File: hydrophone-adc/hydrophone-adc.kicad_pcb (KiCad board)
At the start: 4 copper layers, 204 parts, among them J1001 TEST_1P, J1002 TEST_1P, J1003 TEST_1P, J1004 TEST_1P, J1005 TEST_1P, J1006 TEST_1P, J1007 TEST_1P, J1101 TEST_1P, J1102 TEST_1P, J1201 TEST_1P, J1202 TEST_1P, J1203 TEST_1P, J1204 TEST_1P, J1205 TEST_1P, J1206 TEST_1P, J1207 TEST_1P, J1301 BARREL_JACK, J401 CONN_COAXIAL, J402 CONN_COAXIAL, J403 CONN_COAXIAL, J404 CONN_COAXIAL, J405 TEST_1P, J406 TEST_1P, J407 TEST_1P, J408 TEST_1P, J409 TEST_1P, J410 TEST_1P, J411 TEST_1P, J412 TEST_1P, J501 TEST_1P, J502 TEST_1P, J601 TEST_1P, J602 TEST_1P, J603 TEST_1P, J604 TEST_1P, J605 TEST_1P, J606 TEST_1P, J607 TEST_1P, J701 TEST_1P, J702 TEST_1P, J801 TEST_1P, J802 TEST_1P, J803 TEST_1P, J804 TEST_1P, J805 TEST_1P, J806 TEST_1P, J807 TEST_1P, J901 TEST_1P, J902 TEST_1P, U1001 LM324, U1101 el5170, U1201 LM324, U1301 TS30013, U1302 LM2776, U1303 LT1963, U201 micro-zed-jx1, U301 micro-zed-jx2, U401 LTC2171-14, U501 el5170, U601 LM324, U701 el5170, U801 LM324, U901 el5170

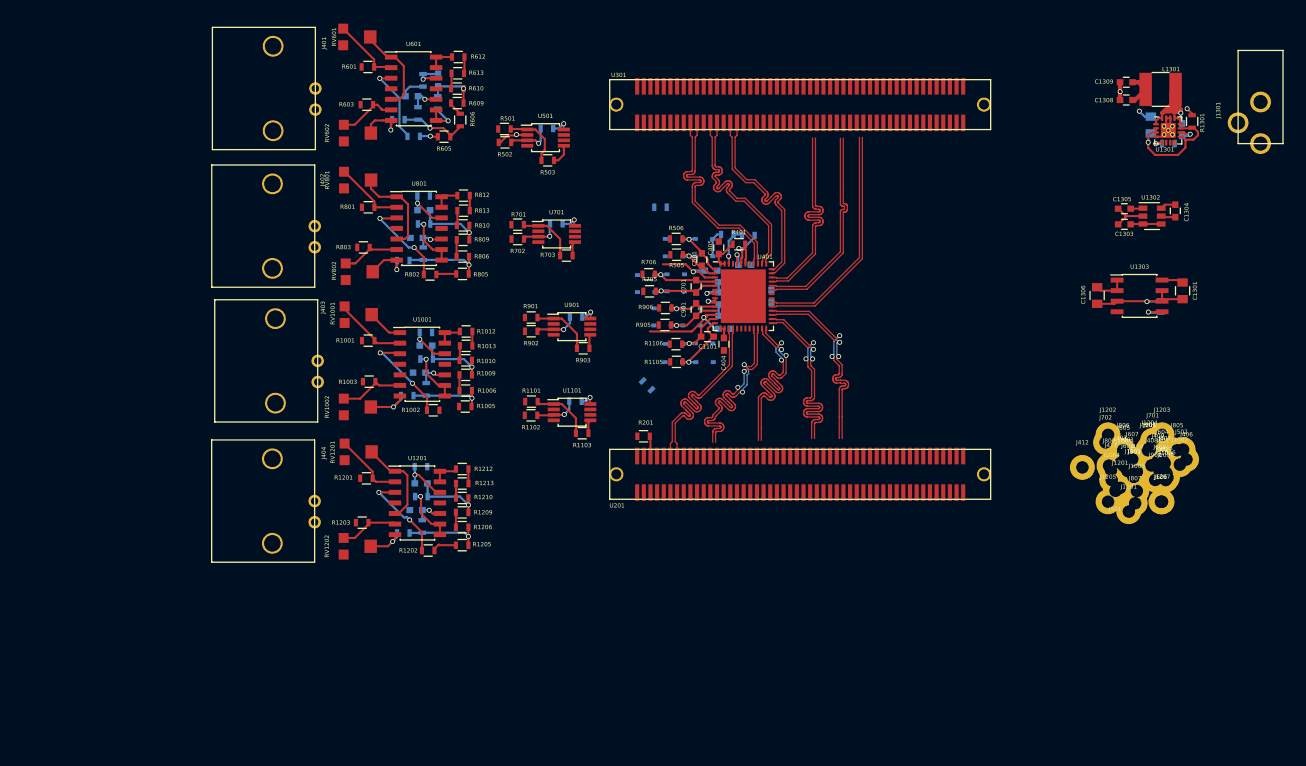
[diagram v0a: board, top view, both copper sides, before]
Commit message: Finished differential routing and plane layout
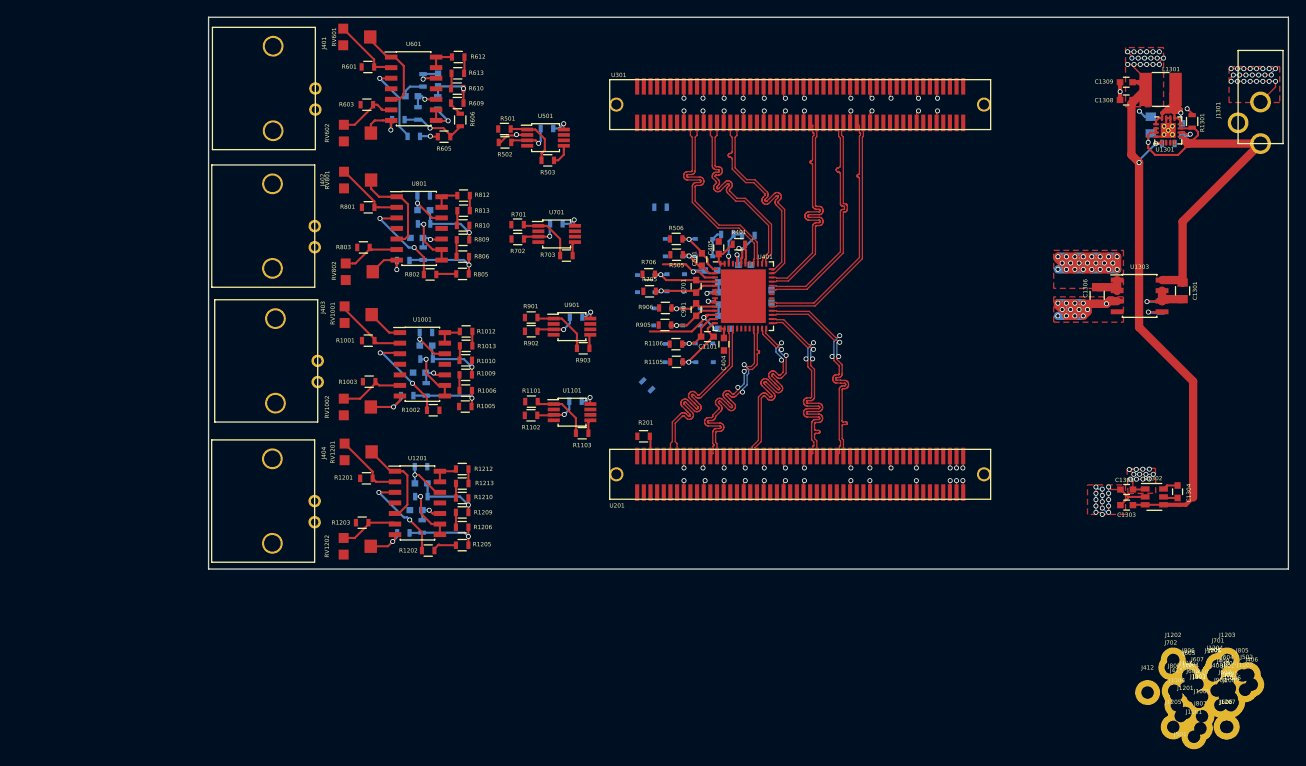
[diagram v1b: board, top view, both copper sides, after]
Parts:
- moved C1304 33.8 mm to (223.2, 97.3)
- moved C1305 33.8 mm to (217.1, 97.1)
- moved C1303 33.8 mm to (217.1, 99.0)
- moved U1302 33.8 mm to (220.4, 98.0)
- moved J1001 28.2 mm to (224.8, 121.2)
- moved J1002 28.2 mm to (231.3, 121.2)
- moved J1005 28.2 mm to (226.1, 124.3)
- moved J1006 28.2 mm to (229.8, 122.7)
- moved J1007 28.2 mm to (224.6, 121.4)
- moved J1204 28.2 mm to (227.7, 119.1)
- moved J1205 28.2 mm to (222.7, 125.6)
- moved J1206 28.2 mm to (227.4, 119.4)
- moved J1207 28.2 mm to (229.1, 125.6)
- moved J406 28.2 mm to (232.1, 120.5)
- moved J502 28.2 mm to (231.7, 119.3)
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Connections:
- U201 pad 23: (no net) -> /out4b+
- U201 pad 25: (no net) -> /out4b-
- U201 pad 35: (no net) -> /out4a+
- U201 pad 37: (no net) -> /out4a-
- U201 pad 53: (no net) -> /out3b+
- U201 pad 55: (no net) -> /out3b-
- U201 pad 61: (no net) -> /out3a+
- U201 pad 63: (no net) -> /out3a-
- U301 pad 36: /out2b+ -> (no net)
- U301 pad 38: /out2b- -> (no net)
- U301 pad 42: /data_clk+ -> (no net)
- U301 pad 44: /data_clk- -> (no net)
- U301 pad 54: (no net) -> /out2b+
- U301 pad 56: (no net) -> /out2b-
- U301 pad 62: /fr_clk+ -> /data_clk+
- U301 pad 64: /fr_clk- -> /data_clk-
- U301 pad 68: /out3a+ -> /fr_clk+
- U301 pad 70: /out3a- -> /fr_clk-
- U301 pad 74: /out3b+ -> (no net)
- U301 pad 76: /out3b- -> (no net)
- U301 pad 82: /out4a+ -> (no net)
- U301 pad 84: /out4a- -> (no net)
- U301 pad 88: /out4b+ -> (no net)
- U301 pad 90: /out4b- -> (no net)
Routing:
- net GND: track 31.5 -> 147.7 mm, vias 5 -> 106
- net +5V: track 9.33 -> 86.7 mm, vias 1 -> 20
- net /Power/Vin: track 18.3 -> 48.3 mm
- net +1V8: track 12.7 -> 36.6 mm, vias 0 -> 23
- net -5V: track 1.50 -> 11.5 mm, vias 0 -> 12
- net /out3b-: track 24.2 -> 27.5 mm
- net /out3a-: track 24.3 -> 27.5 mm
- net /data_clk+: track 24.4 -> 27.0 mm
- net /out2b+: track 24.4 -> 26.9 mm
- net /out3b+: track 25.0 -> 27.5 mm
- net /out3a+: track 25.1 -> 27.5 mm
- net /fr_clk+: track 27.3 -> 29.7 mm
- net /out4a-: track 24.4 -> 26.7 mm
- net /out4a+: track 24.4 -> 26.7 mm
- net /out4b+: track 24.5 -> 26.7 mm
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- added copper zone on F.Cu, net +1V8
- added copper zone on In2.Cu, net +1V8
- added copper zone on F.Cu, net +5V
- added copper zone on In2.Cu, net +5V
- added copper zone on F.Cu, net -5V
- added copper zone on In2.Cu, net -5V
- added copper zone on F.Cu, net GND
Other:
- board outline added: 129.8 x 66.3 mm

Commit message: DRC is now passing and preliminary layout is complete.
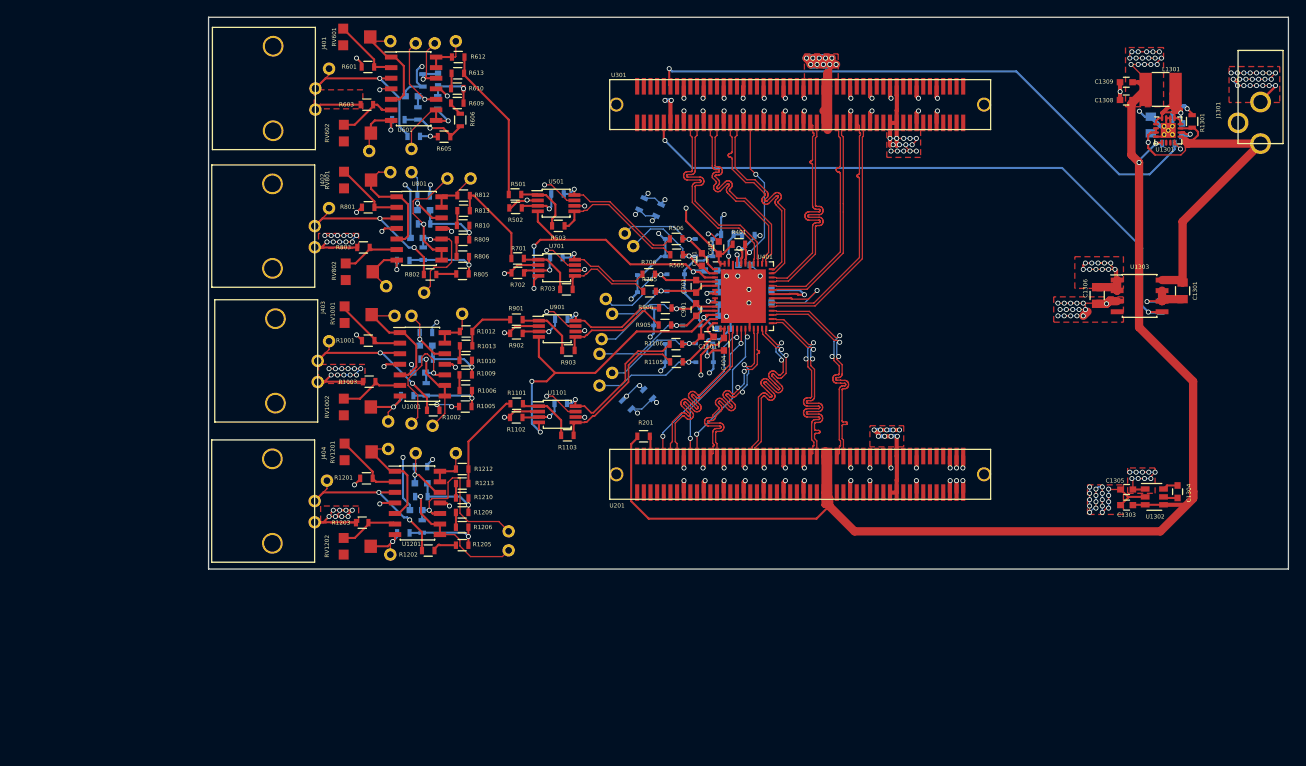
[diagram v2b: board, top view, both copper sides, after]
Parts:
- removed J405, J406, J407, J408, J409, J410, J411, J412: TEST_1P, Measurement_Points:Measurement_Point_Round-TH_Big
- added L403: Ferrite_Bead, Resistors_SMD:R_0603, B.Cu at (157.0, 86.9)
- added L404: Ferrite_Bead, Resistors_SMD:R_0603, B.Cu at (158.8, 62.7)
- J1001, J1002, J1003, J1004, J1005, J1006, J1007, J1101, J1102, J1201, J1202, J1203, J1204, J1205, J1206, J1207, J501, J502, J601, J602, J603, J604, J605, J606, J607, J701, J702, J801, J802, J803, J804, J805, J806, J807, J901, J902: footprint Measurement_Points:Measurement_Point_Round-TH_Big -> Measurement_Points:Measurement_Point_Round-TH_Small
- moved J601 129.1 mm to (121.2, 46.5)
- moved J602 127.6 mm to (128.5, 43.2)
- moved J606 125.7 mm to (133.9, 43.4)
- moved J604 124.2 mm to (131.6, 43.4)
- moved J801 122.7 mm to (121.2, 63.2)
- moved J603 118.7 mm to (126.0, 56.4)
- moved J607 118.0 mm to (136.4, 43.2)
- moved J605 113.1 mm to (131.1, 56.1)
- moved J802 113.0 mm to (128.5, 58.9)
- moved J805 112.7 mm to (135.4, 59.7)
- moved J1001 111.8 mm to (121.2, 79.2)
- moved J1002 111.7 mm to (129.0, 76.2)
- moved J806 111.3 mm to (131.1, 58.9)
- moved J807 109.9 mm to (138.2, 59.7)
- moved J803 109.8 mm to (128.0, 72.6)
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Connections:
- net /ADC/Diff Conv1/Vout+ renamed /ADC/v1+
- net /ADC/Diff Conv1/Vout- renamed /ADC/v1-
- net /ADC/Diff Conv2/Vout+ renamed /ADC/v2+
- net /ADC/Diff Conv2/Vout- renamed /ADC/v2-
- net /ADC/Diff Conv3/Vout+ renamed /ADC/v3+
- net /ADC/Diff Conv3/Vout- renamed /ADC/v3-
- net /ADC/Diff Conv4/Vout+ renamed /ADC/v4+
- net /ADC/Diff Conv4/Vout- renamed /ADC/v4-
- net Net-(R1103-Pad1) renamed /ADC/Diff Conv4/v+
- net Net-(R1104-Pad1) renamed /ADC/Diff Conv4/v-
- net Net-(R503-Pad1) renamed /ADC/Diff Conv1/v+
- net Net-(R504-Pad1) renamed /ADC/Diff Conv1/v-
- net Net-(R703-Pad1) renamed /ADC/Diff Conv2/v+
- net Net-(R704-Pad1) renamed /ADC/Diff Conv2/v-
- net Net-(R903-Pad1) renamed /ADC/Diff Conv3/v+
- net Net-(R904-Pad1) renamed /ADC/Diff Conv3/v-
- J1301 pad 3: (no net) -> Net-(J1301-Pad3)
- R401 pad 2: /ADC/MISO -> /MISO
- RV1001 pad 3: (no net) -> Net-(RV1001-Pad3)
- RV1002 pad 3: (no net) -> Net-(RV1002-Pad3)
- RV1201 pad 3: (no net) -> Net-(RV1201-Pad3)
- RV1202 pad 3: (no net) -> Net-(RV1202-Pad3)
- RV601 pad 3: (no net) -> Net-(RV601-Pad3)
- RV602 pad 3: (no net) -> Net-(RV602-Pad3)
- RV801 pad 3: (no net) -> Net-(RV801-Pad3)
- RV802 pad 3: (no net) -> Net-(RV802-Pad3)
- U201 pad 1: (no net) -> Net-(U201-Pad1)
- U201 pad 10: (no net) -> /MicroZed-JX1/SE1
- U201 pad 12: (no net) -> Net-(U201-Pad12)
- U201 pad 14: (no net) -> Net-(U201-Pad14)
- U201 pad 17: (no net) -> /SCK
- U201 pad 18: (no net) -> Net-(U201-Pad18)
- U201 pad 19: (no net) -> /MOSI
- U201 pad 2: (no net) -> Net-(U201-Pad2)
- U201 pad 20: (no net) -> Net-(U201-Pad20)
- U201 pad 24: (no net) -> Net-(U201-Pad24)
- U201 pad 26: (no net) -> Net-(U201-Pad26)
- U201 pad 29: (no net) -> /MicroZed-JX1/LVDS6+
- U201 pad 3: (no net) -> Net-(U201-Pad3)
- U201 pad 30: (no net) -> Net-(U201-Pad30)
- U201 pad 31: (no net) -> /MicroZed-JX1/LVDS6-
- U201 pad 32: (no net) -> Net-(U201-Pad32)
- U201 pad 36: (no net) -> Net-(U201-Pad36)
- U201 pad 38: (no net) -> Net-(U201-Pad38)
- U201 pad 4: (no net) -> Net-(U201-Pad4)
- U201 pad 41: (no net) -> /MicroZed-JX1/LVDS10+
- U201 pad 42: (no net) -> Net-(U201-Pad42)
- U201 pad 43: (no net) -> /MicroZed-JX1/LVDS10-
- U201 pad 44: (no net) -> Net-(U201-Pad44)
- U201 pad 47: (no net) -> /MicroZed-JX1/LVDS12+
- U201 pad 48: (no net) -> Net-(U201-Pad48)
- U201 pad 49: (no net) -> /MicroZed-JX1/LVDS12-
- U201 pad 50: (no net) -> Net-(U201-Pad50)
- U201 pad 54: (no net) -> Net-(U201-Pad54)
- U201 pad 56: (no net) -> Net-(U201-Pad56)
- U201 pad 6: (no net) -> Net-(U201-Pad6)
- U201 pad 62: (no net) -> Net-(U201-Pad62)
- U201 pad 64: (no net) -> Net-(U201-Pad64)
- U201 pad 67: (no net) -> /MicroZed-JX1/LVDS18+
- U201 pad 68: (no net) -> Net-(U201-Pad68)
- U201 pad 69: (no net) -> /MicroZed-JX1/LVDS18-
- U201 pad 7: (no net) -> Net-(U201-Pad7)
- U201 pad 70: (no net) -> Net-(U201-Pad70)
- U201 pad 73: (no net) -> /MicroZed-JX1/LVDS20+
- U201 pad 74: (no net) -> Net-(U201-Pad74)
- U201 pad 75: (no net) -> /MicroZed-JX1/LVDS20-
- U201 pad 76: (no net) -> Net-(U201-Pad76)
- U201 pad 8: (no net) -> Net-(U201-Pad8)
- U201 pad 81: (no net) -> Net-(U201-Pad81)
- U201 pad 82: (no net) -> Net-(U201-Pad82)
- U201 pad 83: (no net) -> Net-(U201-Pad83)
- U201 pad 84: (no net) -> Net-(U201-Pad84)
- U201 pad 87: (no net) -> Net-(U201-Pad87)
- U201 pad 88: (no net) -> Net-(U201-Pad88)
- U201 pad 89: (no net) -> Net-(U201-Pad89)
- U201 pad 9: (no net) -> /~CS
- U201 pad 90: (no net) -> Net-(U201-Pad90)
- U201 pad 91: (no net) -> Net-(U201-Pad91)
- U201 pad 92: (no net) -> Net-(U201-Pad92)
- U201 pad 93: (no net) -> Net-(U201-Pad93)
- U201 pad 94: (no net) -> Net-(U201-Pad94)
- U301 pad 1: (no net) -> Net-(U301-Pad1)
- U301 pad 100: (no net) -> Net-(U301-Pad100)
- U301 pad 13: (no net) -> Net-(U301-Pad13)
- U301 pad 14: (no net) -> Net-(U301-Pad14)
- U301 pad 17: (no net) -> Net-(U301-Pad17)
- U301 pad 19: (no net) -> Net-(U301-Pad19)
- U301 pad 2: (no net) -> Net-(U301-Pad2)
- U301 pad 23: (no net) -> Net-(U301-Pad23)
- U301 pad 25: (no net) -> Net-(U301-Pad25)
- U301 pad 29: (no net) -> Net-(U301-Pad29)
- U301 pad 3: (no net) -> Net-(U301-Pad3)
- U301 pad 31: (no net) -> Net-(U301-Pad31)
- U301 pad 35: (no net) -> Net-(U301-Pad35)
- U301 pad 36: (no net) -> /MISO
- U301 pad 37: (no net) -> Net-(U301-Pad37)
- U301 pad 38: (no net) -> /MicroZed-JX2/LVDS7-
- U301 pad 4: (no net) -> Net-(U301-Pad4)
- U301 pad 41: (no net) -> Net-(U301-Pad41)
- U301 pad 42: (no net) -> /MicroZed-JX2/LVDS9+
- U301 pad 43: (no net) -> Net-(U301-Pad43)
- U301 pad 44: (no net) -> /MicroZed-JX2/LVDS9-
- U301 pad 47: (no net) -> Net-(U301-Pad47)
- U301 pad 48: (no net) -> /MicroZed-JX2/LVDS11+
- U301 pad 49: (no net) -> Net-(U301-Pad49)
- U301 pad 5: (no net) -> Net-(U301-Pad5)
- U301 pad 50: (no net) -> /MicroZed-JX2/LVDS11-
- U301 pad 53: (no net) -> Net-(U301-Pad53)
- U301 pad 55: (no net) -> Net-(U301-Pad55)
- U301 pad 6: (no net) -> Net-(U301-Pad6)
- U301 pad 61: (no net) -> Net-(U301-Pad61)
- U301 pad 63: (no net) -> Net-(U301-Pad63)
- U301 pad 67: (no net) -> Net-(U301-Pad67)
- U301 pad 69: (no net) -> Net-(U301-Pad69)
- U301 pad 7: (no net) -> Net-(U301-Pad7)
- U301 pad 73: (no net) -> Net-(U301-Pad73)
- U301 pad 74: (no net) -> /MicroZed-JX2/LVDS19+
- U301 pad 75: (no net) -> Net-(U301-Pad75)
- U301 pad 76: (no net) -> /MicroZed-JX2/LVDS19-
- U301 pad 8: (no net) -> Net-(U301-Pad8)
- U301 pad 81: (no net) -> Net-(U301-Pad81)
- U301 pad 82: (no net) -> Net-(U301-Pad82)
- U301 pad 83: (no net) -> Net-(U301-Pad83)
- U301 pad 84: (no net) -> Net-(U301-Pad84)
- U301 pad 87: (no net) -> Net-(U301-Pad87)
- U301 pad 88: (no net) -> Net-(U301-Pad88)
- U301 pad 89: (no net) -> Net-(U301-Pad89)
- U301 pad 9: (no net) -> Net-(U301-Pad9)
- U301 pad 90: (no net) -> Net-(U301-Pad90)
- U301 pad 93: (no net) -> Net-(U301-Pad93)
- U301 pad 94: (no net) -> Net-(U301-Pad94)
- U301 pad 95: (no net) -> Net-(U301-Pad95)
- U301 pad 96: (no net) -> Net-(U301-Pad96)
- U301 pad 97: (no net) -> Net-(U301-Pad97)
- U301 pad 98: (no net) -> Net-(U301-Pad98)
- U301 pad 99: (no net) -> Net-(U301-Pad99)
- U401 pad 19: (no net) -> /~CS
- U401 pad 20: (no net) -> /SCK
- U401 pad 21: (no net) -> /MOSI
- U401 pad 46: /ADC/MISO -> /MISO
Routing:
- net GNDREF: track 6.78 -> 155.0 mm, vias 1 -> 61
- net +5V: track 86.7 -> 233.9 mm, vias 20 -> 38
- net /vccio_en: track 3.19 -> 76.3 mm, vias 1 -> 2
- net /v_good: track 0.00 -> 72.2 mm, vias 0 -> 2
- net +1V8: track 36.6 -> 101.7 mm, vias 23 -> 39
- net GND: track 147.7 -> 190.0 mm, vias 106 -> 117
- net /ADC/Vcm34: track 11.7 -> 41.2 mm, vias 1 -> 3
- net /ADC/Vcm12: track 8.37 -> 36.5 mm, vias 1 -> 3
- net -5V: track 11.5 -> 32.0 mm, vias 12 -> 17
- net /MISO: track 0.00 -> 20.1 mm, vias 0 -> 2
- net /~CS: track 0.00 -> 19.3 mm, vias 0 -> 2
- net /MOSI: track 0.00 -> 18.0 mm, vias 0 -> 2
- net Net-(C1201-Pad1): track 3.51 -> 21.5 mm
- net /SCK: track 0.00 -> 17.9 mm, vias 0 -> 2
- net /ADC/Diff Conv1/Vin: track 2.38 -> 19.2 mm
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- added copper zone on F.Cu, net GNDREF

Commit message: Added in higher stacking and moved BNCs forward
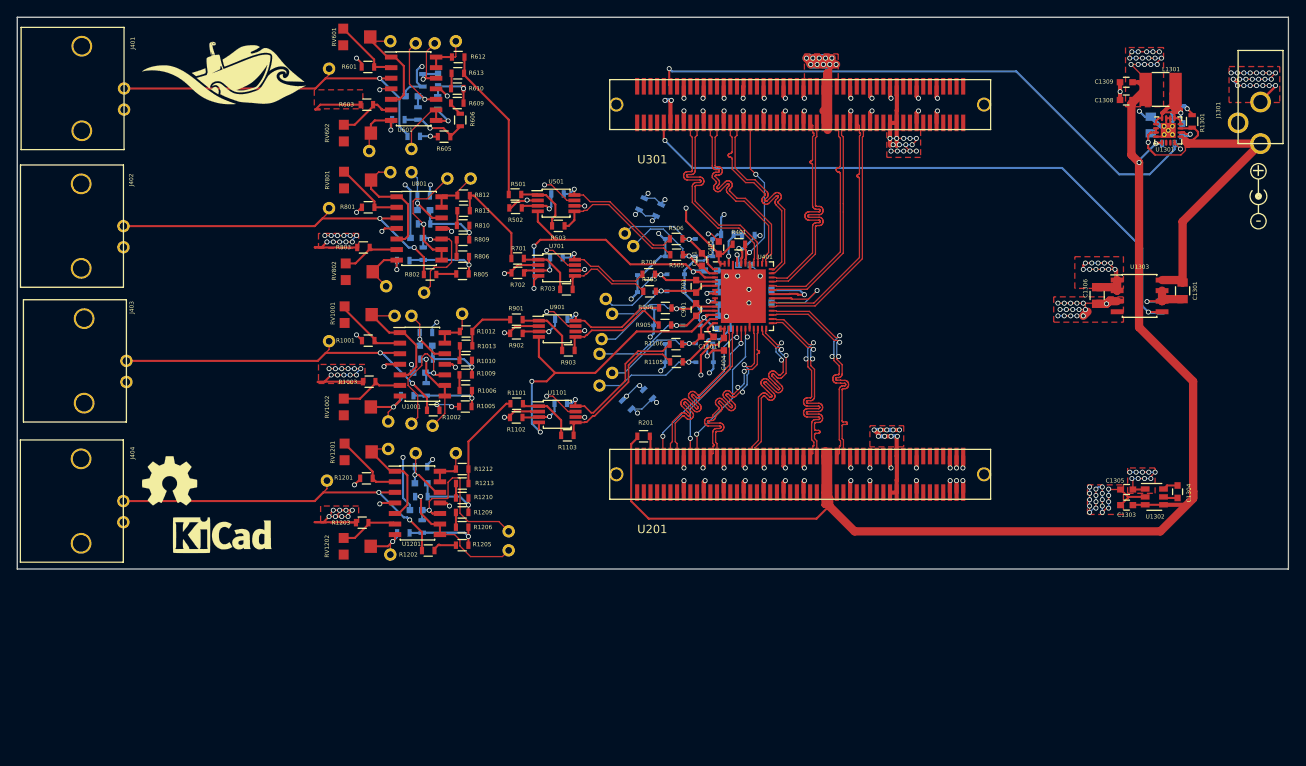
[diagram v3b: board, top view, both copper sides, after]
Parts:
- added G***: LOGO, robosub_footprints:robosub_logo-large, F.Cu at (108.7, 47.2)
- added REF**: Symbol_Barrel_Polarity, Symbols:Symbol_Barrel_Polarity, F.Cu at (232.8, 61.8)
- added REF**: KiCAD Logo, Symbols:Symbol_KiCAD-Logo_CopperAndSilkScreenTop, F.Cu at (108.3, 102.4)
- added REF***: OSHW-Symbol_6.7x6mm_SilkScreen, Symbols:OSHW-Symbol_6.7x6mm_SilkScreen, F.Cu at (102.0, 96.0)
- moved J401 23.0 mm to (96.5, 48.9)
- moved J402 23.0 mm to (96.4, 65.4)
- moved J403 23.0 mm to (96.8, 81.6)
- moved J404 23.0 mm to (96.4, 98.5)
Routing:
- net /ADC/Filter3/Vin: track 22.6 -> 45.6 mm
- net /ADC/Filter1/Vin: track 21.0 -> 44.0 mm
- net /ADC/Filter4/Vin: track 22.5 -> 45.5 mm
- net /ADC/Filter2/Vin: track 22.4 -> 45.4 mm
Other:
- board size 129.8 x 66.3 mm -> 152.8 x 66.3 mm
- board text added: "+"
- board text added: "-"
- board text added: "Hydropone ADC Ryan Summers Rev A"
